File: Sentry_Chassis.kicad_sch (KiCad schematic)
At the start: 21 parts, among them J1 FR_CAN, J10 Y2_CAN, J11 Y1_XT30, J12 Y2_XT30, J13 UART, J14 SWD, J15 CAN1, J16 CAN2, J17 Ref, J2 FR_XT30, J3 FL_CAN, J4 FL_XT30, J5 BR_CAN, J6 BR_XT30, J7 BL_CAN, J8 BL_XT30, J9 Y1_CAN

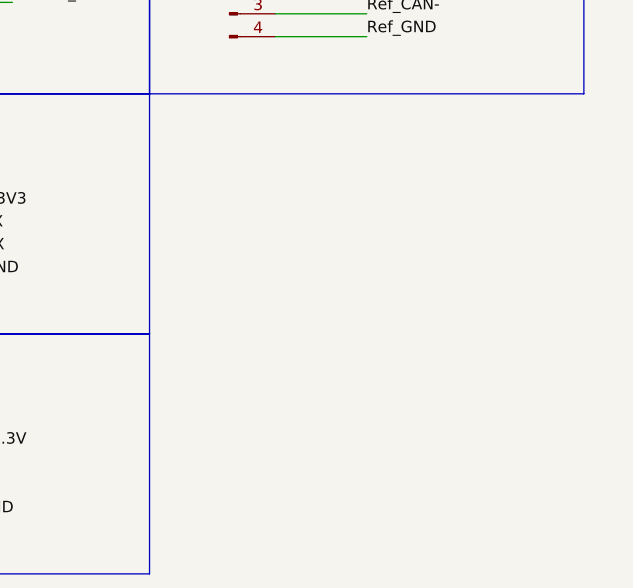
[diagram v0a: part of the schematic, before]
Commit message: 16 pin connector labeled
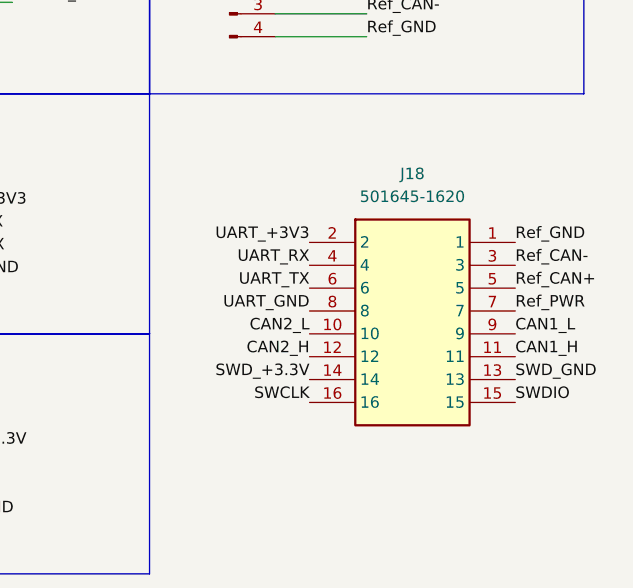
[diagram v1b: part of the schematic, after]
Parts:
- added J18: 501645-1620, 5016451620, symbol Robomaster_Library:501645-1620
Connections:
- net CAN1_H: now also J18.11
- net CAN1_L: now also J18.9
- net CAN2_H: now also J18.12
- net CAN2_L: now also J18.10
- net Ref_CAN+: now also J18.5
- net Ref_CAN-: now also J18.3
- net Ref_GND: now also J18.1
- net Ref_PWR: now also J18.7
- net SWCLK: now also J18.16
- net SWDIO: now also J18.15
- net SWD_+3.3V: now also J18.14
- net SWD_GND: now also J18.13
- net UART_+3V3: now also J18.2
- net UART_GND: now also J18.8
- net UART_RX: now also J18.4
- net UART_TX: now also J18.6
